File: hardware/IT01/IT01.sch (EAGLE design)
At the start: 10 parts

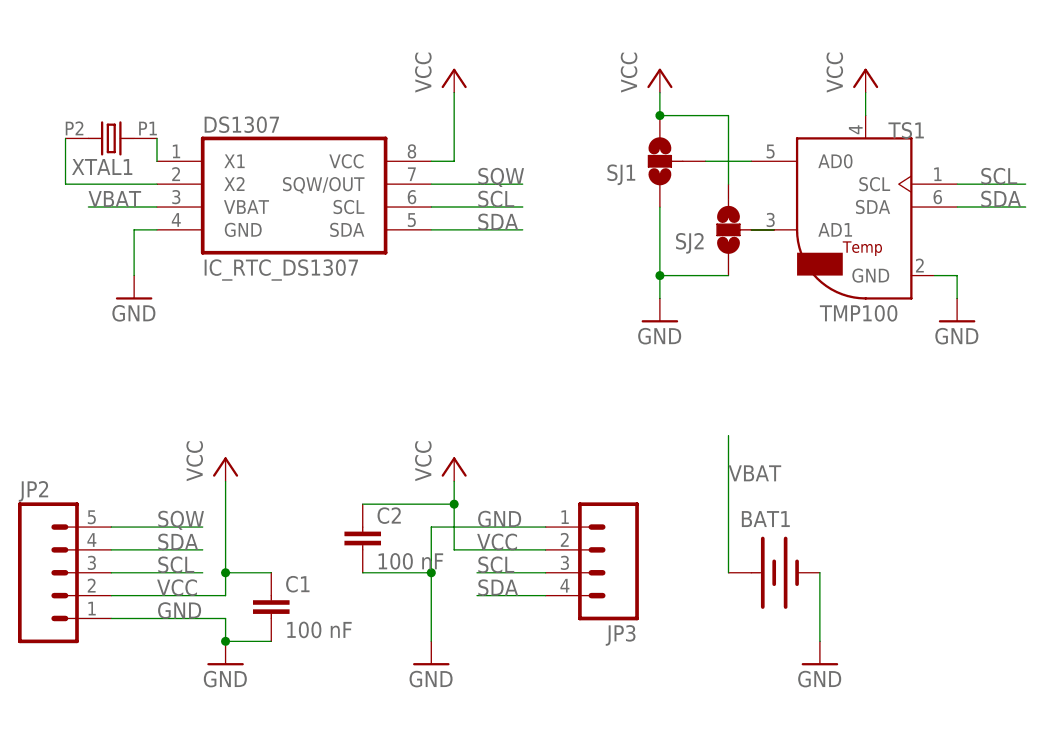
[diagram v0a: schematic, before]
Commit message: IT01 for Seeedstudio
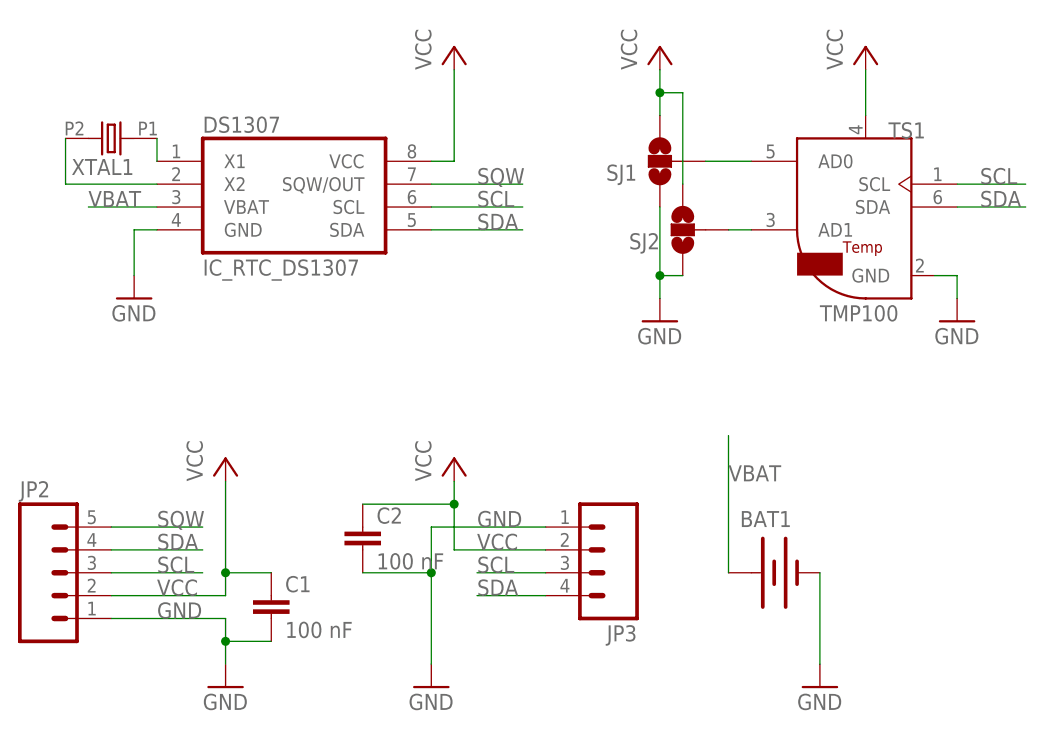
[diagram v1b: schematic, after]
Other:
- moved on the sheet: SJ2
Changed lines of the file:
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@@
 <instance part="JP3" gate="G$1" x="12.7" y="48.26" rot="R180"/>
 <instance part="SJ1" gate="G$1" x="20.32" y="91.44" rot="R180"/>
-<instance part="SJ2" gate="G$1" x="27.94" y="83.82" rot="R180"/>
+<instance part="SJ2" gate="G$1" x="22.86" y="83.82" rot="R180"/>
 <instance part="TS1" gate="G$1" x="35.56" y="93.98"/>
 <instance part="DS1307" gate="G$1" x="-20.32" y="86.36"/>
 <instance part="XTAL1" gate="X" x="-40.64" y="93.98" rot="R180"/>
 <instance part="JP2" gate="G$1" x="-48.26" y="45.72"/>
-<instance part="GND1" gate="1" x="-27.94" y="35.56"/>
+<instance part="GND1" gate="1" x="-27.94" y="33.02"/>
 <instance part="P+1" gate="VCC" x="-27.94" y="58.42"/>
-<instance part="GND2" gate="1" x="-5.08" y="35.56"/>
+<instance part="GND2" gate="1" x="-5.08" y="33.02"/>
 <instance part="P+2" gate="VCC" x="-2.54" y="58.42"/>
 <instance part="BAT1" gate="G$1" x="33.02" y="45.72"/>
-<instance part="GND3" gate="1" x="38.1" y="35.56"/>
+<instance part="GND3" gate="1" x="38.1" y="33.02"/>
 <instance part="C1" gate="G$1" x="-22.86" y="43.18"/>
-<instance part="P+4" gate="VCC" x="-2.54" y="101.6"/>
+<instance part="P+4" gate="VCC" x="-2.54" y="104.14"/>
 <instance part="GND4" gate="1" x="-38.1" y="76.2"/>
 <instance part="C2" gate="G$1" x="-12.7" y="50.8"/>
-<instance part="P+3" gate="VCC" x="20.32" y="101.6"/>
+<instance part="P+3" gate="VCC" x="20.32" y="104.14"/>
 <instance part="GND5" gate="1" x="20.32" y="73.66"/>
 <instance part="GND6" gate="1" x="53.34" y="73.66"/>
-<instance part="P+5" gate="VCC" x="43.18" y="101.6"/>
+<instance part="P+5" gate="VCC" x="43.18" y="104.14"/>
 </instances>
 <busses>
@@
 <pinref part="GND1" gate="1" pin="GND"/>
 <wire x1="-27.94" y1="40.64" x2="-27.94" y2="38.1" width="0.1524" layer="91"/>
+<wire x1="-27.94" y1="38.1" x2="-27.94" y2="35.56" width="0.1524" layer="91"/>
 <wire x1="-27.94" y1="40.64" x2="-40.64" y2="40.64" width="0.1524" layer="91"/>
 <pinref part="JP2" gate="G$1" pin="1"/>
@@
 <wire x1="-5.08" y1="50.8" x2="-5.08" y2="45.72" width="0.1524" layer="91"/>
 <pinref part="C2" gate="G$1" pin="2"/>
-<wire x1="-5.08" y1="45.72" x2="-5.08" y2="38.1" width="0.1524" layer="91"/>
+<wire x1="-5.08" y1="45.72" x2="-5.08" y2="35.56" width="0.1524" layer="91"/>
 <wire x1="-12.7" y1="45.72" x2="-5.08" y2="45.72" width="0.1524" layer="91"/>
 <junction x="-5.08" y="45.72"/>
@@
 <pinref part="BAT1" gate="G$1" pin="-"/>
 <pinref part="GND3" gate="1" pin="GND"/>
-<wire x1="38.1" y1="45.72" x2="38.1" y2="38.1" width="0.1524" layer="91"/>
+<wire x1="38.1" y1="45.72" x2="38.1" y2="35.56" width="0.1524" layer="91"/>
 </segment>
 <segment>
@@
 <pinref part="SJ2" gate="G$1" pin="1"/>
 <wire x1="20.32" y1="78.74" x2="20.32" y2="86.36" width="0.1524" layer="91"/>
-<wire x1="27.94" y1="78.74" x2="20.32" y2="78.74" width="0.1524" layer="91"/>
+<wire x1="22.86" y1="78.74" x2="20.32" y2="78.74" width="0.1524" layer="91"/>
 <junction x="20.32" y="78.74"/>
 </segment>
@@
 <pinref part="P+4" gate="VCC" pin="VCC"/>
 <wire x1="-5.08" y1="91.44" x2="-2.54" y2="91.44" width="0.1524" layer="91"/>
-<wire x1="-2.54" y1="91.44" x2="-2.54" y2="99.06" width="0.1524" layer="91"/>
+<wire x1="-2.54" y1="91.44" x2="-2.54" y2="101.6" width="0.1524" layer="91"/>
 </segment>
 <segment>
 <pinref part="SJ1" gate="G$1" pin="3"/>
 <pinref part="P+3" gate="VCC" pin="VCC"/>
+<wire x1="20.32" y1="101.6" x2="20.32" y2="99.06" width="0.1524" layer="91"/>
+<pinref part="SJ2" gate="G$1" pin="3"/>
 <wire x1="20.32" y1="99.06" x2="20.32" y2="96.52" width="0.1524" layer="91"/>
-<pinref part="SJ2" gate="G$1" pin="3"/>
-<wire x1="27.94" y1="88.9" x2="27.94" y2="96.52" width="0.1524" layer="91"/>
-<wire x1="27.94" y1="96.52" x2="20.32" y2="96.52" width="0.1524" layer="91"/>
-<junction x="20.32" y="96.52"/>
+<wire x1="22.86" y1="88.9" x2="22.86" y2="99.06" width="0.1524" layer="91"/>
+<wire x1="22.86" y1="99.06" x2="20.32" y2="99.06" width="0.1524" layer="91"/>
+<junction x="20.32" y="99.06"/>
 </segment>
 <segment>
 <pinref part="TS1" gate="G$1" pin="UCC"/>
 <pinref part="P+5" gate="VCC" pin="VCC"/>
-<wire x1="43.18" y1="99.06" x2="43.18" y2="96.52" width="0.1524" layer="91"/>
+<wire x1="43.18" y1="101.6" x2="43.18" y2="96.52" width="0.1524" layer="91"/>
 </segment>
 </net>
@@
 <pinref part="SJ2" gate="G$1" pin="2"/>
 <pinref part="TS1" gate="G$1" pin="AD1"/>
-<wire x1="33.02" y1="83.82" x2="30.48" y2="83.82" width="0.1524" layer="91"/>
-</segment>
-</net>
+<wire x1="27.94" y1="83.82" x2="30.48" y2="83.82" width="0.1524" layer="91"/>
+</segment>
+</net>
